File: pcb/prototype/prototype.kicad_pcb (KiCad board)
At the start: 2 copper layers, 35 parts, among them J1 GS2, J10 Conn_01x14, J11 Conn_01x14, J2 GS2, J3 GS2, J4 GS2, J5 GS2, J6 GS2, J7 GS2, J8 GS2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

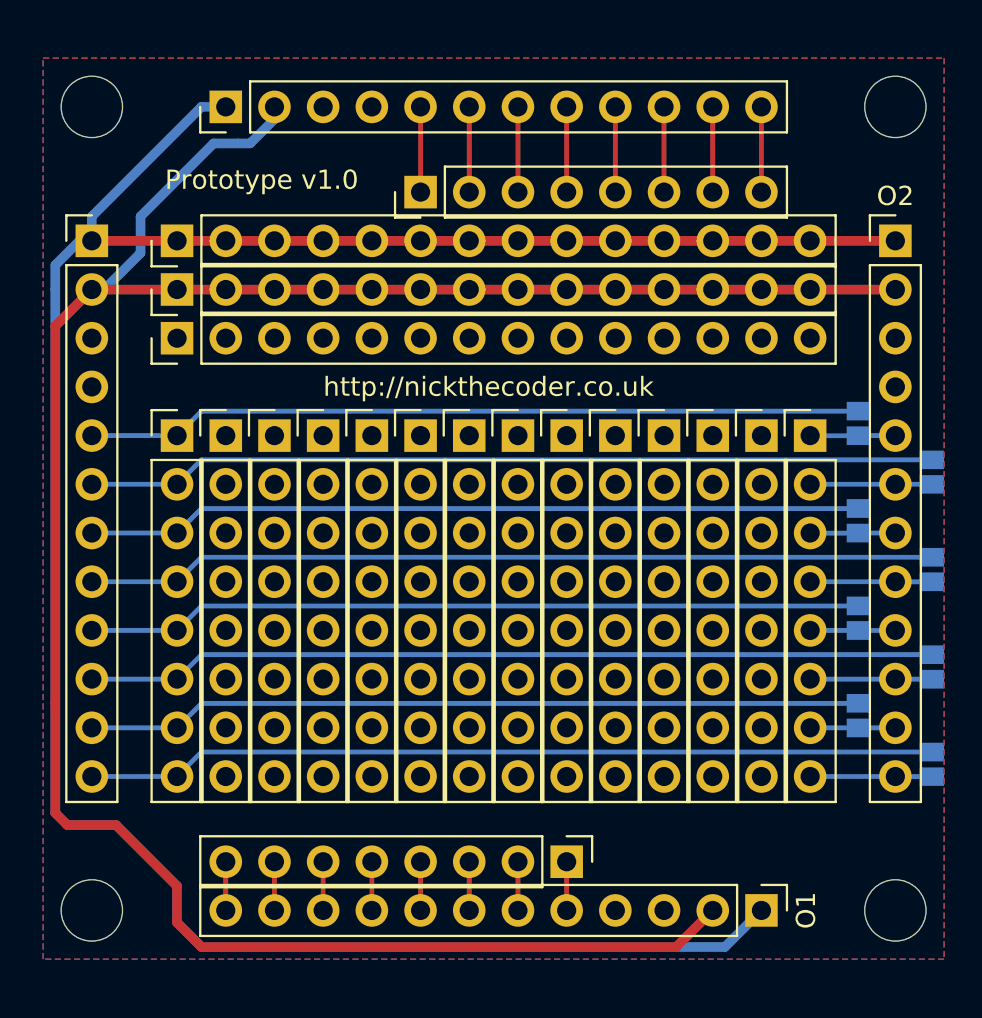
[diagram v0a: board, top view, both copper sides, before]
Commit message: Improved ioExpansion
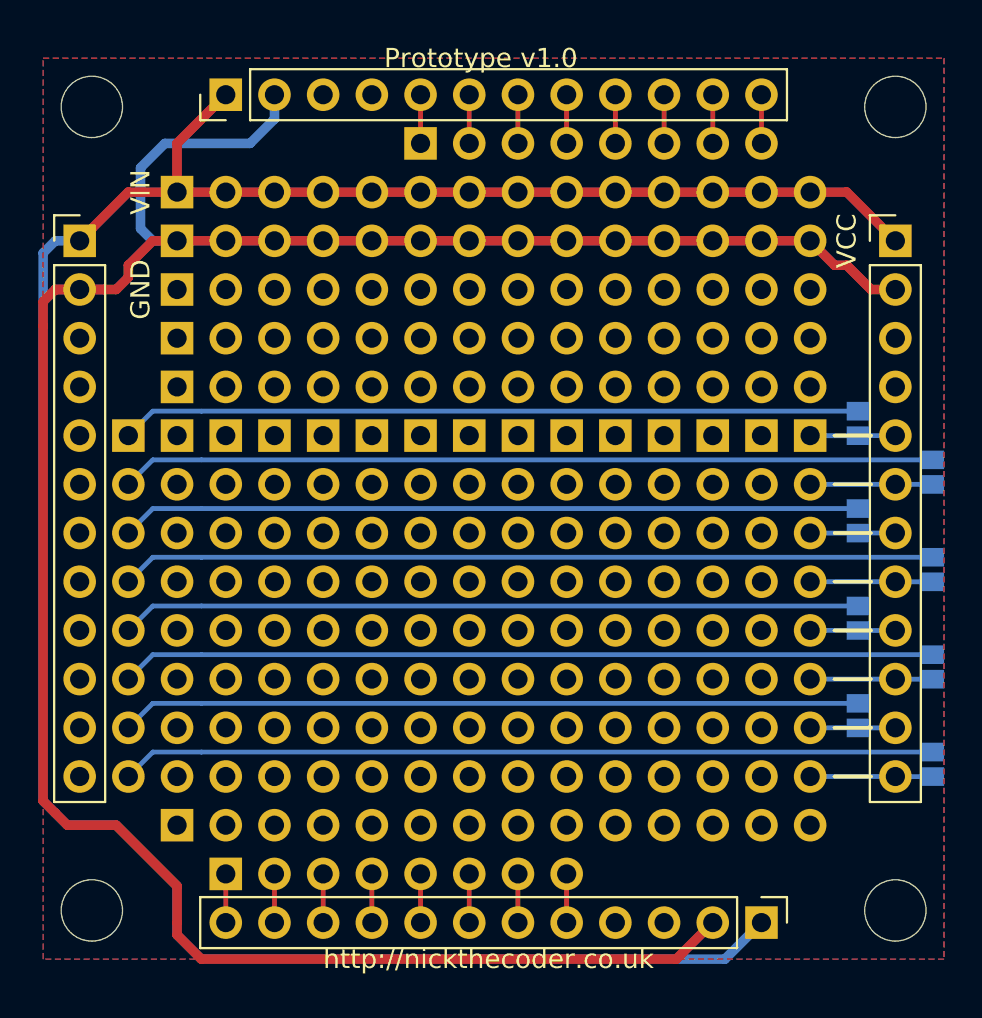
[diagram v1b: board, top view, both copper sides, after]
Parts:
- removed H2: Headers8L, Pin_Headers:Pin_Header_Straight_1x08_Pitch2.54mm
- removed H3: Headers8, Pin_Headers:Pin_Header_Straight_1x08_Pitch2.54mm
- added J12: Conn_01x08, Pin_Headers:Pin_Header_Straight_1x08_Pitch2.54mm, B.Cu at (134.0, 125.7)
- added J13: Conn_01x08, Pin_Headers:Pin_Header_Straight_1x08_Pitch2.54mm, B.Cu at (144.1, 87.6)
- added REF**: Pin_Header_Straight_1x08_Pitch2.54mm, Pin_Headers:Pin_Header_Straight_1x08_Pitch2.54mm, B.Cu at (131.4, 102.9)
- added REF**: Pin_Header_Straight_1x08_Pitch2.54mm, Pin_Headers:Pin_Header_Straight_1x14_Pitch2.54mm, B.Cu at (131.4, 123.2)
- added REF**: Pin_Header_Straight_1x08_Pitch2.54mm, Pin_Headers:Pin_Header_Straight_1x14_Pitch2.54mm, B.Cu at (131.4, 97.8)
- added REF**: Pin_Header_Straight_1x08_Pitch2.54mm, Pin_Headers:Pin_Header_Straight_1x14_Pitch2.54mm, B.Cu at (131.4, 100.3)
- H1, H4, J10, J11, J9, REF** (x12): moved to B.Cu
- moved J10 2.54 mm to (131.4, 92.7), turned to 270 degrees
- moved J9 2.54 mm to (131.4, 95.2), turned to 270 degrees
- moved H1 2.54 mm to (128.9, 102.9), turned to 180 degrees
- moved J11 2.54 mm to (131.4, 90.2), turned to 270 degrees
- moved I1 0.64 mm to (126.4, 92.7)
- moved O1 0.64 mm to (161.9, 128.3)
- moved I2 0.63 mm to (134.0, 85.1)
- turned H4 to 180 degrees
- turned REF** to 180 degrees (x7)
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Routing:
- net /VCC: track 124.7 -> 130.4 mm
- net Net-(I2-Pad9): track 4.45 -> 2.54 mm
- net Net-(I2-Pad8): track 4.45 -> 2.54 mm
- net Net-(I2-Pad7): track 4.45 -> 2.54 mm
- net Net-(I2-Pad6): track 4.45 -> 2.54 mm
- net Net-(I2-Pad5): track 4.45 -> 2.54 mm
- net Net-(I2-Pad12): track 4.45 -> 2.54 mm
- net Net-(I2-Pad11): track 4.45 -> 2.54 mm
- net Net-(I2-Pad10): track 4.45 -> 2.54 mm
- net /L7: track 44.3 -> 42.4 mm
- net /L6: track 40.5 -> 38.6 mm
- net /L5: track 44.3 -> 42.4 mm
- net /L4: track 40.5 -> 38.6 mm
- net /L3: track 44.3 -> 42.4 mm
- net /L2: track 40.5 -> 38.6 mm
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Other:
- board text added: "Enable"
- board text added: "GND"
- board text added: "Passthrough"
- board text added: "VCC"
- board text added: "VIN"

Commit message: Ready for the second batch of PCBs to be printed.
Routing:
- net /L7: track 42.4 -> 45.0 mm
- net /L6: track 38.6 -> 41.2 mm
- net /L5: track 42.4 -> 45.0 mm
- net /L4: track 38.6 -> 41.2 mm
- net /L3: track 42.4 -> 45.0 mm
- net /L2: track 38.6 -> 41.2 mm
- net /L1: track 42.4 -> 45.0 mm
- net /L0: track 38.6 -> 41.2 mm
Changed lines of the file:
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@@
   (general
     (links 99)
-    (no_connects 8)
-    (area 123.19 81.915 172.720001 131.71)
+    (no_connects 0)
+    (area 123.19 81.915 172.720001 131.445001)
     (thickness 1.6)
     (drawings 15)
-    (tracks 151)
+    (tracks 159)
     (zones 0)
     (modules 39)
@@
   (segment (start 127 92.075) (end 128.905 90.17) (width 0.5) (layer F.Cu) (net 1))
   (segment (start 128.905 90.17) (end 131.445 90.17) (width 0.5) (layer F.Cu) (net 1))
+  (segment (start 126.365 102.87) (end 128.905 102.87) (width 0.25) (layer F.Cu) (net 3))
   (segment (start 167.005 101.595) (end 132.72 101.595) (width 0.25) (layer B.Cu) (net 3))
   (segment (start 132.72 101.595) (end 130.18 101.595) (width 0.25) (layer B.Cu) (net 3))
   (segment (start 130.18 101.595) (end 128.905 102.87) (width 0.25) (layer B.Cu) (net 3))
+  (segment (start 126.365 105.41) (end 128.905 105.41) (width 0.25) (layer F.Cu) (net 4))
   (segment (start 170.815 104.135) (end 132.72 104.135) (width 0.25) (layer B.Cu) (net 4))
   (segment (start 132.72 104.135) (end 130.18 104.135) (width 0.25) (layer B.Cu) (net 4))
   (segment (start 130.18 104.135) (end 128.905 105.41) (width 0.25) (layer B.Cu) (net 4))
+  (segment (start 126.365 107.95) (end 128.905 107.95) (width 0.25) (layer F.Cu) (net 5))
   (segment (start 132.715 106.675) (end 130.18 106.675) (width 0.25) (layer B.Cu) (net 5))
   (segment (start 130.18 106.675) (end 128.905 107.95) (width 0.25) (layer B.Cu) (net 5))
   (segment (start 167.005 106.675) (end 132.715 106.675) (width 0.25) (layer B.Cu) (net 5))
+  (segment (start 126.365 110.49) (end 128.905 110.49) (width 0.25) (layer F.Cu) (net 6))
   (segment (start 132.72 109.215) (end 130.18 109.215) (width 0.25) (layer B.Cu) (net 6))
   (segment (start 130.175 109.22) (end 128.905 110.49) (width 0.25) (layer B.Cu) (net 6))
   (segment (start 130.18 109.215) (end 130.175 109.22) (width 0.25) (layer B.Cu) (net 6))
   (segment (start 170.815 109.215) (end 132.72 109.215) (width 0.25) (layer B.Cu) (net 6))
+  (segment (start 126.365 113.03) (end 128.905 113.03) (width 0.25) (layer F.Cu) (net 7))
   (segment (start 132.72 111.755) (end 130.18 111.755) (width 0.25) (layer B.Cu) (net 7))
   (segment (start 130.18 111.755) (end 128.905 113.03) (width 0.25) (layer B.Cu) (net 7))
   (segment (start 167.005 111.755) (end 132.72 111.755) (width 0.25) (layer B.Cu) (net 7))
+  (segment (start 126.365 115.57) (end 128.905 115.57) (width 0.25) (layer F.Cu) (net 8))
   (segment (start 132.715 114.295) (end 130.18 114.295) (width 0.25) (layer B.Cu) (net 8))
   (segment (start 130.18 114.295) (end 128.905 115.57) (width 0.25) (layer B.Cu) (net 8))
   (segment (start 170.815 114.295) (end 132.715 114.295) (width 0.25) (layer B.Cu) (net 8))
+  (segment (start 126.365 118.11) (end 128.905 118.11) (width 0.25) (layer F.Cu) (net 9))
   (segment (start 132.72 116.835) (end 130.18 116.835) (width 0.25) (layer B.Cu) (net 9))
   (segment (start 130.18 116.835) (end 128.905 118.11) (width 0.25) (layer B.Cu) (net 9))
   (segment (start 167.005 116.835) (end 132.72 116.835) (width 0.25) (layer B.Cu) (net 9))
+  (segment (start 126.365 120.65) (end 128.905 120.65) (width 0.25) (layer F.Cu) (net 10))
   (segment (start 130.18 119.375) (end 128.905 120.65) (width 0.25) (layer B.Cu) (net 10))
   (segment (start 132.715 119.375) (end 130.18 119.375) (width 0.25) (layer B.Cu) (net 10))
